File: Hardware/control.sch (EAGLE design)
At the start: 11 parts, among them IC1 317T

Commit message: Added some better schematics
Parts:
- removed C1: 100uF, Rodentometer:C-EU050-024X044
- removed C2: 100uF, Rodentometer:C-EU075-032X103
- removed JP3: (no value), Rodentometer:PINHD-1X4
- added ARDUINO_DATA: (no value), Rodentometer:PINHD-1X6
- added LCD: (no value), Rodentometer:PINHD-1X4
- added R6: 10k, Rodentometer:R-EU_0207/7
- added RESET_SWITCH: (no value), Rodentometer:PINHD-1X2
- added SENSOR, SWITCHES: (no value), Rodentometer:PINHD-1X3
- R3: device Rodentometer:R-EU_0204/7 -> Rodentometer:R-EU_0207/10
- renumbered JP1 to ARDUINO_POWER, JP2 to POWER
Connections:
- net N$2 renamed VCC
- removed net N$1: ARDUINO_POWER.1, IC1.VO, R1.1
- removed net N$3: C2.1, JP3.1, R3.2
- removed net N$4: C1.1, JP3.2, R4.2
- removed net N$6: ARDUINO_POWER.6, JP3.3, R5.1
- new net HALL: ARDUINO_DATA.5, R6.1, SENSOR.3
- new net LCD_RX: ARDUINO_DATA.4, LCD.4
- new net LCD_TX: ARDUINO_DATA.3, LCD.3
- new net RESET: ARDUINO_POWER.6, R5.1, RESET_SWITCH.1
- new net SW_A: ARDUINO_DATA.1, R3.1, SWITCHES.1
- new net SW_B: ARDUINO_DATA.2, R4.1, SWITCHES.2
- new net VIN: ARDUINO_POWER.1, IC1.VO, LCD.1, R1.1
- net +5V: now also SENSOR.1, SWITCHES.3; no longer R3.1, R4.1
- net GND: now also LCD.2, R3.2, R4.2, R6.2, RESET_SWITCH.2, SENSOR.2; no longer C1.2, C2.2, JP3.4
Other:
- moved on the sheet: R3, R4, R5

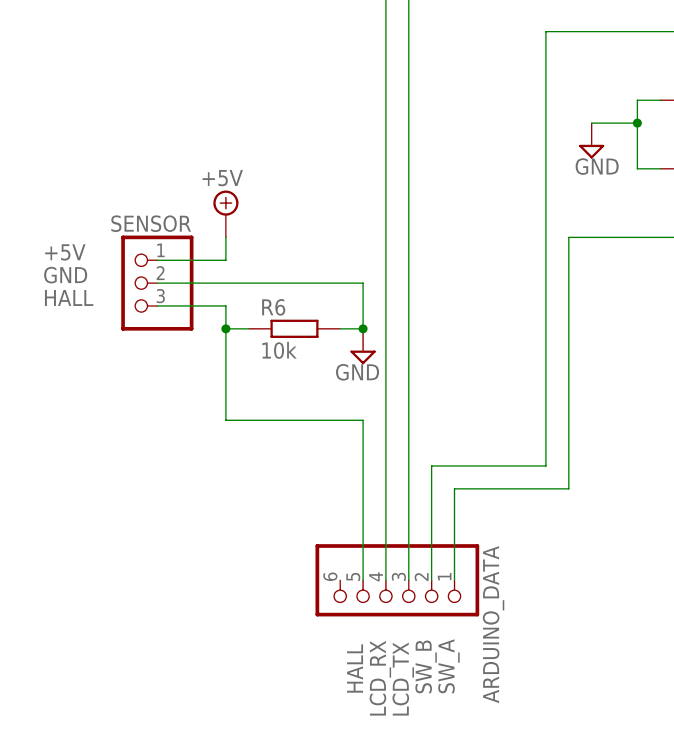
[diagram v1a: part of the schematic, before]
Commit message: Fixed error in schematics and updated code to use Interrupt
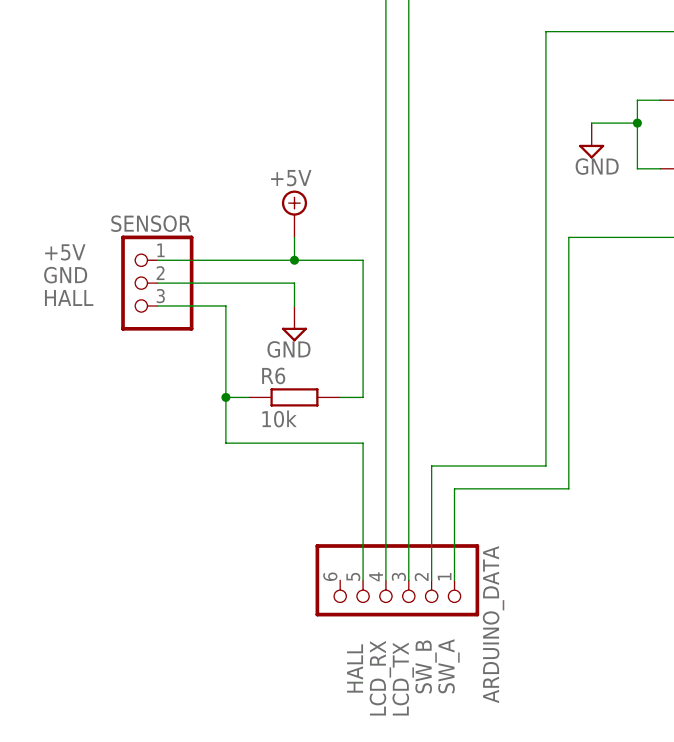
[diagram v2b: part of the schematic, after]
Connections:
- net +5V: now also R6.2
- net GND: no longer R6.2
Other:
- moved on the sheet: R6
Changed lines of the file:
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@@
 <instance part="RESET_SWITCH" gate="G$1" x="114.3" y="48.26"/>
 <instance part="SENSOR" gate="A" x="22.86" y="-2.54" rot="MR0"/>
-<instance part="SUPPLY4" gate="GND" x="48.26" y="-10.16" rot="MR0"/>
-<instance part="SUPPLY6" gate="+5V" x="33.02" y="5.08" rot="MR0"/>
-<instance part="R6" gate="G$1" x="40.64" y="-7.62"/>
+<instance part="SUPPLY4" gate="GND" x="40.64" y="-7.62" rot="MR0"/>
+<instance part="SUPPLY6" gate="+5V" x="40.64" y="5.08" rot="MR0"/>
+<instance part="R6" gate="G$1" x="40.64" y="-15.24"/>
 </instances>
 <busses>
@@
 <segment>
 <pinref part="SENSOR" gate="A" pin="2"/>
-<wire x1="25.4" y1="-2.54" x2="48.26" y2="-2.54" width="0.1524" layer="91"/>
-<wire x1="48.26" y1="-2.54" x2="48.26" y2="-7.62" width="0.1524" layer="91"/>
+<wire x1="25.4" y1="-2.54" x2="40.64" y2="-2.54" width="0.1524" layer="91"/>
+<wire x1="40.64" y1="-2.54" x2="40.64" y2="-5.08" width="0.1524" layer="91"/>
 <pinref part="SUPPLY4" gate="GND" pin="GND"/>
-<pinref part="R6" gate="G$1" pin="2"/>
-<wire x1="45.72" y1="-7.62" x2="48.26" y2="-7.62" width="0.1524" layer="91"/>
-<junction x="48.26" y="-7.62"/>
 <label x="12.7" y="-2.54" size="1.778" layer="95"/>
 </segment>
@@
 <segment>
 <pinref part="SENSOR" gate="A" pin="1"/>
-<wire x1="25.4" y1="0" x2="33.02" y2="0" width="0.1524" layer="91"/>
-<wire x1="33.02" y1="0" x2="33.02" y2="2.54" width="0.1524" layer="91"/>
+<wire x1="25.4" y1="0" x2="40.64" y2="0" width="0.1524" layer="91"/>
+<wire x1="40.64" y1="0" x2="40.64" y2="2.54" width="0.1524" layer="91"/>
 <pinref part="SUPPLY6" gate="+5V" pin="+5V"/>
 <label x="12.7" y="0" size="1.778" layer="95"/>
+<pinref part="R6" gate="G$1" pin="2"/>
+<wire x1="45.72" y1="-15.24" x2="48.26" y2="-15.24" width="0.1524" layer="91"/>
+<wire x1="48.26" y1="-15.24" x2="48.26" y2="0" width="0.1524" layer="91"/>
+<wire x1="48.26" y1="0" x2="40.64" y2="0" width="0.1524" layer="91"/>
+<junction x="40.64" y="0"/>
 </segment>
 <segment>
@@
 <pinref part="SENSOR" gate="A" pin="3"/>
 <wire x1="25.4" y1="-5.08" x2="33.02" y2="-5.08" width="0.1524" layer="91"/>
-<wire x1="33.02" y1="-7.62" x2="33.02" y2="-17.78" width="0.1524" layer="91"/>
-<wire x1="33.02" y1="-17.78" x2="48.26" y2="-17.78" width="0.1524" layer="91"/>
+<wire x1="33.02" y1="-15.24" x2="33.02" y2="-20.32" width="0.1524" layer="91"/>
+<wire x1="33.02" y1="-20.32" x2="48.26" y2="-20.32" width="0.1524" layer="91"/>
 <pinref part="ARDUINO_DATA" gate="A" pin="5"/>
-<wire x1="48.26" y1="-17.78" x2="48.26" y2="-35.56" width="0.1524" layer="91"/>
+<wire x1="48.26" y1="-20.32" x2="48.26" y2="-35.56" width="0.1524" layer="91"/>
 <label x="48.26" y="-48.26" size="1.778" layer="95" rot="R90"/>
-<wire x1="33.02" y1="-5.08" x2="33.02" y2="-7.62" width="0.1524" layer="91"/>
+<wire x1="33.02" y1="-5.08" x2="33.02" y2="-15.24" width="0.1524" layer="91"/>
 <pinref part="R6" gate="G$1" pin="1"/>
-<wire x1="33.02" y1="-7.62" x2="35.56" y2="-7.62" width="0.1524" layer="91"/>
-<junction x="33.02" y="-7.62"/>
+<wire x1="33.02" y1="-15.24" x2="35.56" y2="-15.24" width="0.1524" layer="91"/>
+<junction x="33.02" y="-15.24"/>
 <label x="12.7" y="-5.08" size="1.778" layer="95"/>
 </segment>

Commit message: Added some screenshots ready for blogging
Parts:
- R1: value 220 -> 220R
- R5: value (none) -> 100R
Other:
- moved on the sheet: ARDUINO_DATA, ARDUINO_POWER, IC1, LCD, POWER, R1, R2, R3, R4, R5, R6, RESET_SWITCH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
